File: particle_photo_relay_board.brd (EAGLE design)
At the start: 100 x 80 mm, 12 parts, among them Q1 600mA/40V

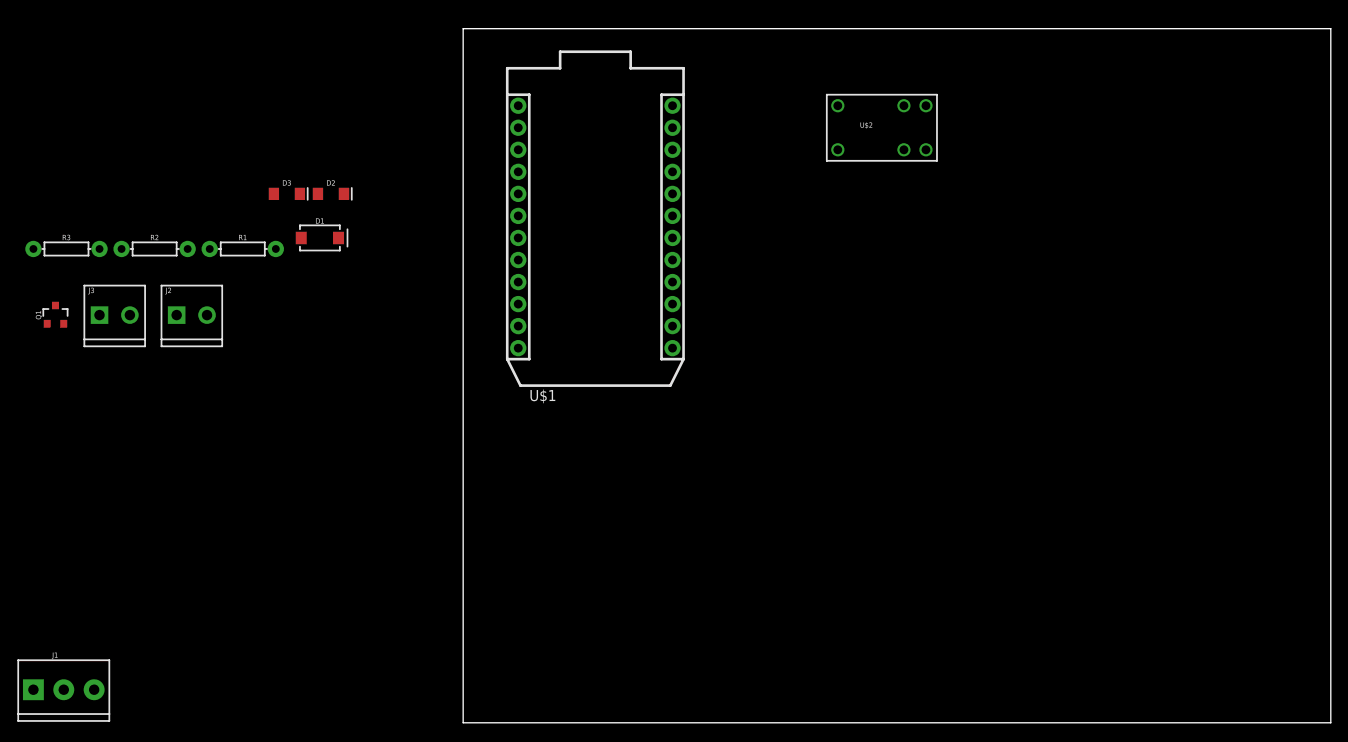
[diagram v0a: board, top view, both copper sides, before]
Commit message: Laid out a pelim draft of the board
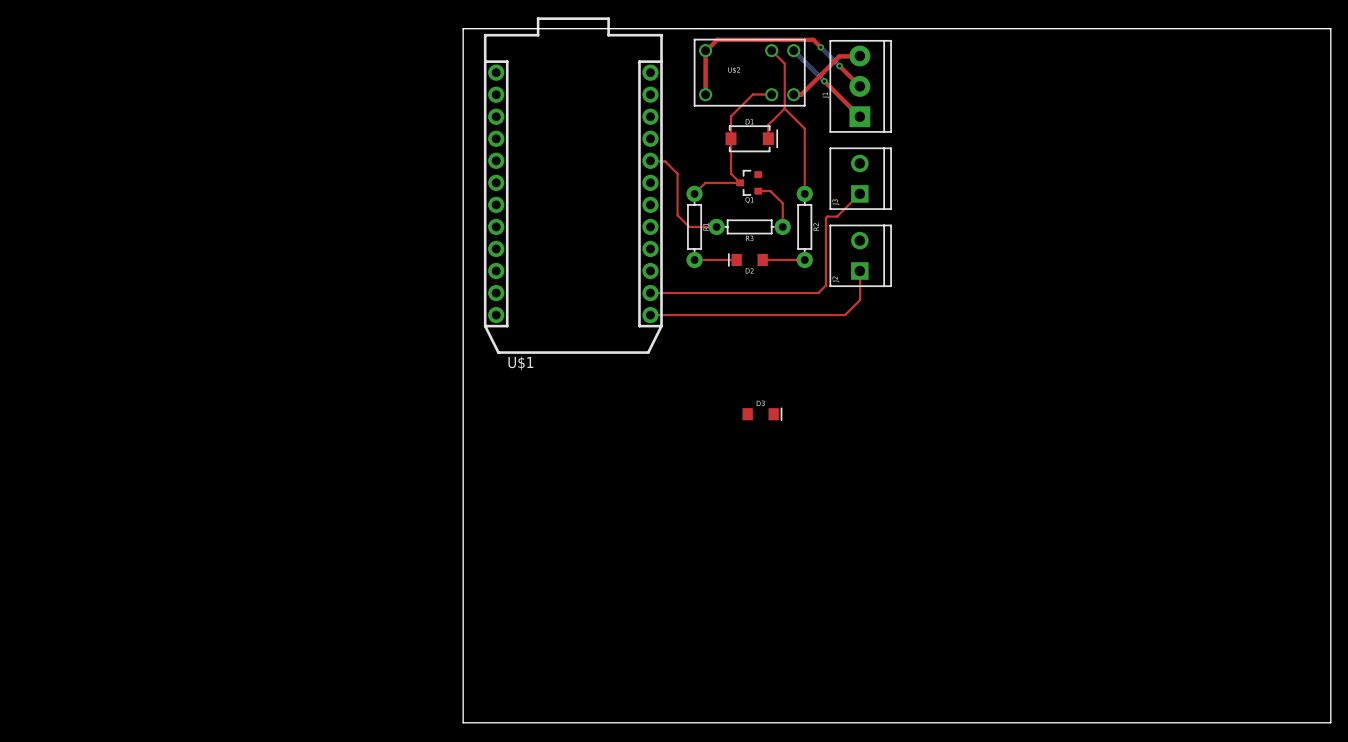
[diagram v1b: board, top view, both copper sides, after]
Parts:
- moved J1 115.9 mm to (45.7, 69.8), turned to 90 degrees
- moved J3 88.7 mm to (45.7, 61.0), turned to 90 degrees
- moved Q1 81.4 mm to (33.0, 62.2), turned to 90 degrees
- moved J2 78.9 mm to (45.7, 52.1), turned to 90 degrees
- moved R3 78.8 mm to (33.0, 57.1), turned to 180 degrees
- moved R2 75.0 mm to (39.4, 57.1), turned to 270 degrees
- moved D3 60.2 mm to (34.3, 35.6)
- moved R1 52.1 mm to (26.7, 57.1), turned to 270 degrees
- moved D1 50.8 mm to (33.0, 67.3)
- moved D2 48.9 mm to (33.0, 53.3), turned to 180 degrees
- moved U$2 16.5 mm to (33.0, 74.9)
- moved U$1 4.58 mm to (2.54, 41.9)
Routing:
- net N$10: track 0.00 -> 33.4 mm
- net N$6: track 0.00 -> 28.2 mm
- net N$9: track 0.00 -> 25.6 mm, vias 0 -> 2
- net N$2: track 0.00 -> 22.4 mm
- net N$1: track 0.00 -> 19.6 mm
- net N$5: track 0.00 -> 13.6 mm
- net N$7: track 0.00 -> 10.8 mm, vias 0 -> 1
- net N$8: track 0.00 -> 9.47 mm
- net N$4: track 0.00 -> 6.11 mm
- net N$3: track 0.00 -> 4.85 mm
- net VCC: track 0.00 -> 4.85 mm

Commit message: Add files via upload
P.R.A.C.C REV1 SCH and BRD files ready for review.
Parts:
- removed D3: GREEN, SparkFun-LED:LED-1206
- removed J1: (no value), SparkFun-Connectors:SCREWTERMINAL-3.5MM-3
- removed J2, J3: (no value), SparkFun-Retired:SCREWTERMINAL-3.5MM-2
- added C1, C2: 1uF, rcl:C0805
- added J4, J5: (no value), SparkFun-Connectors:SCREWTERMINAL-5MM-3
- added R4, R7: 0, rcl:R0805
- added R5, R6: 0 - DNI, rcl:R0805
- added U2: MIC5219BM5, v-reg-micrel:SOT23-5
- R1: value (none) -> 330; device SparkFun-Resistors:AXIAL-0.3 -> rcl:R0805
- R2, R3: value (none) -> 10; device SparkFun-Resistors:AXIAL-0.3 -> rcl:R0805
- U$2: value RELAY-SPDT-2-G5V -> RELAYOMRON; device SparkFun-Retired:RELAY-G5V -> Particle:G5LE-14-DC5
- moved D1 22.0 mm to (29.2, 45.7)
- moved D2 21.1 mm to (22.7, 35.0), turned to 90 degrees
- moved R3 20.2 mm to (18.4, 43.2)
- moved U$2 20.1 mm to (24.7, 56.6)
- moved Q1 18.9 mm to (23.8, 45.7), turned to 270 degrees
- moved R2 18.1 mm to (31.6, 40.7)
- moved R1 16.5 mm to (25.4, 40.7)
- moved U$1 12.0 mm to (3.73, 30.0), turned to 270 degrees
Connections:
- removed net 3V3: U$1.24
- removed net N$10: J3.1, U$1.14
- removed net N$5: R3.P$2, U$1.20
- removed net N$6: J2.1, U$1.13
- removed net N$7: J1.1, U$2.1
- removed net N$8: J1.3, U$2.10
- removed net N$9: J1.2, U$2.5, U$2.6
- removed net VCC: D2.A, R2.P$2
- removed net VIN: U$1.1
- new net 3V3_BACKUP: C2.1, R6.1, U2.5
- new net 3V3_PHOTON: R5.1, U$1.24
- new net COM: J4.2, U$2.COMMON
- new net NC: J4.3, U$2.CLOSED
- new net NO: J4.1, U$2.OPEN
- new net PHOTON_D0: J5.2, U$1.13
- new net PHOTON_D1: J5.3, U$1.14
- new net PHOTON_D7: R3.2, U$1.20
- new net VBUS_BACKUP: C1.1, R7.1, U2.1
- new net VCOIL: D2.A, R2.2, R4.2, R5.2, R6.2
- new net VIN_PHOTON: R4.1, R7.2, U$1.1
- net GND: now also C1.2, C2.2, J5.1, U2.2
- net N$1: now also R1.1, U$2.COIL2; no longer R1.P$1, U$2.9
- net N$2: now also R2.1, U$2.COIL1; no longer R2.P$1, U$2.2
- net N$3: now also R1.2; no longer R1.P$2
- net N$4: now also R3.1; no longer R3.P$1
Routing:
- net PHOTON_D7: track 0.00 -> 37.1 mm
- net N$10: track 33.4 -> 0.00 mm
- net 3V3_PHOTON: track 0.00 -> 32.7 mm, vias 0 -> 2
- net COM: track 0.00 -> 29.0 mm
- net N$6: track 28.2 -> 0.00 mm
- net N$9: track 25.6 -> 0.00 mm, vias 2 -> 0
- net VCOIL: track 0.00 -> 16.8 mm
- net NO: track 0.00 -> 14.8 mm
- net NC: track 0.00 -> 14.4 mm
- net N$5: track 13.6 -> 0.00 mm
- net VIN_PHOTON: track 0.00 -> 12.8 mm
- net N$7: track 10.8 -> 0.00 mm, vias 1 -> 0
- net PHOTON_D1: track 0.00 -> 10.2 mm
- net 3V3_BACKUP: track 0.00 -> 9.86 mm
- net N$8: track 9.47 -> 0.00 mm
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- added copper zone on layer 1, net GND
- added copper zone on layer 16, net GND
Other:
- board size 100 x 80 mm -> 45 x 65 mm
- board text added: "P.R.A.C.C."
- board text added: "REV1"
